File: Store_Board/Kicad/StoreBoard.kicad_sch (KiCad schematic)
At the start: 42 parts, among them J1 Conn_01x10, J2 Conn_01x10, J3 Conn_01x10, J4 Conn_01x10, U1 HM62256BLP, U2 74HCT574, U3 74HCT574, U4 74HCT04, U417 74LS00, U418 74LS00, U419 74LS08, U420 74HC04, U421 74LS112, U422 SN74LS74, U423 74LS10, U424 74LS32

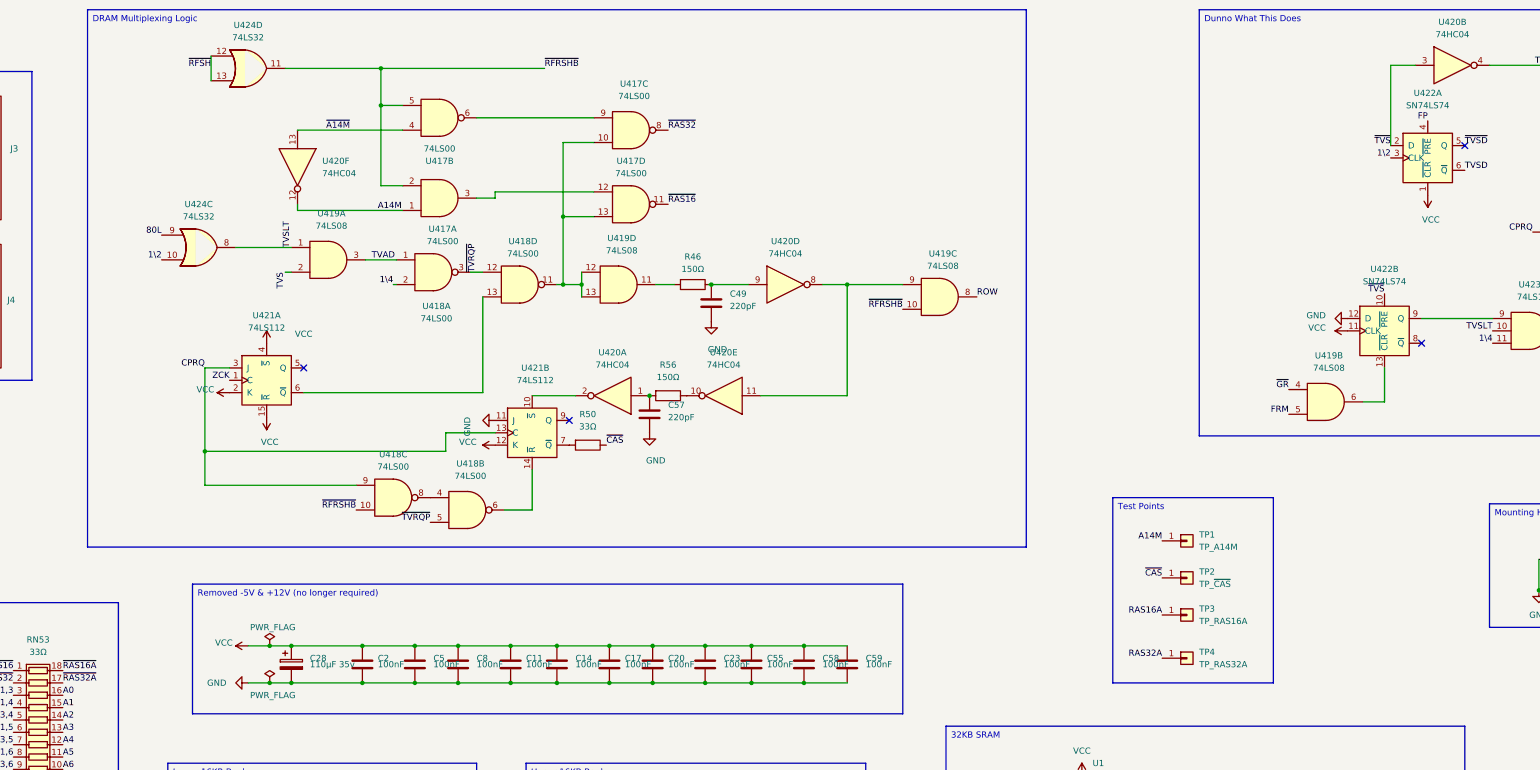
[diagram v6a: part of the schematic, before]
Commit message: Added testpoints
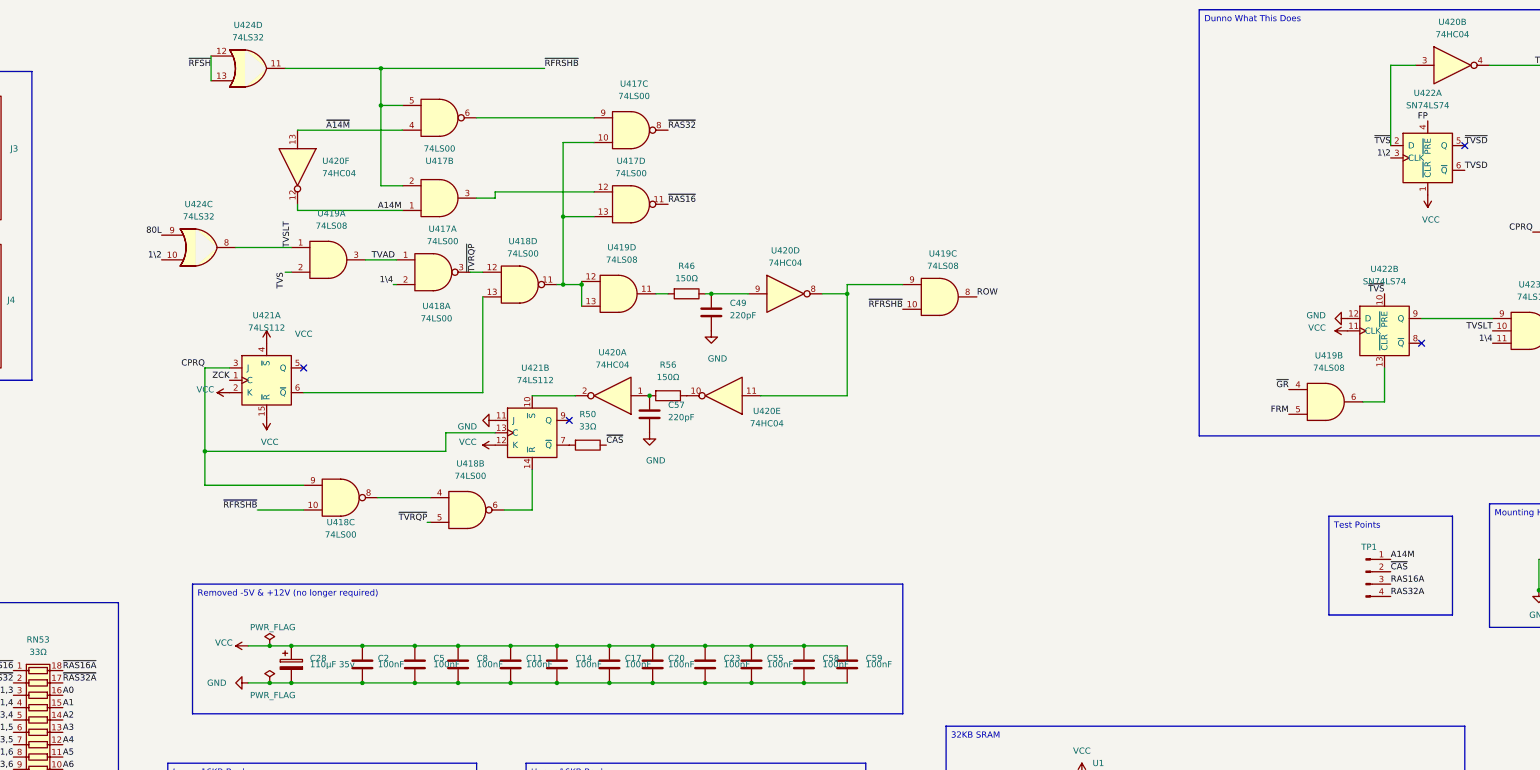
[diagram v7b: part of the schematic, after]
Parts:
- removed TP1: TP_A14M, TestPoint:TestPoint_THTPad_D2.0mm_Drill1.0mm, symbol Connector_Generic:Conn_01x01
- removed TP2: TP_~{CAS}, TestPoint:TestPoint_THTPad_D2.0mm_Drill1.0mm, symbol Connector_Generic:Conn_01x01
- removed TP3: TP_RAS16A, TestPoint:TestPoint_THTPad_D2.0mm_Drill1.0mm, symbol Connector_Generic:Conn_01x01
- removed TP4: TP_RAS32A, TestPoint:TestPoint_THTPad_D2.0mm_Drill1.0mm, symbol Connector_Generic:Conn_01x01
- added TP1: Conn_01x04_Pin, Connector_PinHeader_2.54mm:PinHeader_1x04_P2.54mm_Vertical, symbol Connector:Conn_01x04_Pin
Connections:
- net A14M: now also TP1.1 (Pin_1)
- net RAS16A: now also TP1.3 (Pin_3)
- net RAS32A: now also TP1.4 (Pin_4)
- net ~{CAS}: now also TP1.2 (Pin_2)
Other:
- moved on the sheet: C49, R46, U418C, U419D, U420D

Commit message: Further refinements
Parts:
- removed R50: 33Ω, Resistor_THT:R_Axial_DIN0204_L3.6mm_D1.6mm_P5.08mm_Horizontal, symbol Device:R
- removed RN52: 33Ω, Package_DIP:DIP-16_W7.62mm, symbol Device:R_Pack08
- removed RN53: 33Ω, Package_DIP:DIP-18_W7.62mm, symbol Device:R_Pack09
- removed TP1: Conn_01x04_Pin, Connector_PinHeader_2.54mm:PinHeader_1x04_P2.54mm_Vertical, symbol Connector:Conn_01x04_Pin
- removed U3: 74HCT574, Package_DIP:DIP-20_W7.62mm, symbol 74xx:74HCT574
- removed unit 2 of U4
- added TP1: Conn_02x05_Odd_Even, Connector_PinHeader_2.54mm:PinHeader_2x05_P2.54mm_Vertical, symbol Connector_Generic:Conn_02x05_Odd_Even
- added U3: 74LS32, Package_DIP:DIP-14_W7.62mm, symbol 74xx:74LS32
- C28: value 110µF 35v -> 10µF 35v
- U2: value 74HCT574 -> 74LS574
- U4: value 74HCT04 -> 74LS04
- U420: value 74HC04 -> 74LS04
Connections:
- net RAS_A14 is gone; now on net A14M: U1.1 (A14)
- net ~{RAS16A} is gone; now on net ~{RAS16}: U4.1
- net A14M: now also TP1.1 (Pin_1)
- net GND: now also TP1.10 (Pin_10), TP1.2 (Pin_2), TP1.4 (Pin_4), TP1.6 (Pin_6), TP1.8 (Pin_8), U3.10, U3.12, U3.13, U3.4, U3.5, U3.7 (GND), U3.9; no longer U4.5
- net M1,1: now also RN54.5 (R4), U1.15 (Q3)
- net M2,10: now also RN54.7 (R6), U1.17 (Q5)
- net M4,10: now also RN54.6 (R5), U1.16 (Q4)
- net M4,3: now also RN54.9 (R8), U1.19 (Q7)
- net M4,6: now also RN54.2 (R1), U1.11 (Q0)
- net M4,7: now also RN54.3 (R2), U1.12 (Q1)
- net M4,8: now also RN54.4 (R3), U1.13 (Q2)
- net M4,9: now also RN54.8 (R7), U1.18 (Q6)
- net VCC: now also U3.14 (VCC); no longer RN54.1 (common)
- net ~{CAS}: now also U421.7 (~{Q}), TP1.3 (Pin_3)
- net ~{RAS32}: now also U4.5
- net RAS32: now reaches U4.6
- net RAS32: now also TP1.9 (Pin_9), U3.2
- removed net D0: RN54.9 (R8), U1.11 (Q0)
- removed net D1: RN54.8 (R7), U1.12 (Q1)
- removed net D2: RN54.7 (R6), U1.13 (Q2)
- removed net D3: RN54.6 (R5), U1.15 (Q3)
- removed net D4: RN54.5 (R4), U1.16 (Q4)
- removed net D5: RN54.4 (R3), U1.17 (Q5)
- removed net D6: RN54.3 (R2), U1.18 (Q6)
- removed net D7: RN54.2 (R1), U1.19 (Q7)
- net RAS16A renamed RAS
- net RAS: now also TP1.5 (Pin_5), U3.3; no longer U4.2
- new net RAS16: TP1.7 (Pin_7), U3.1, U4.2
- no-connect marks 10 -> 16
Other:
- note removed: "Or should we use ~{A14M} signal here?"
- note removed: "Use RAS32 to address upper 16KB bank a la A14"
- moved on the sheet: C57, HOLE1, HOLE2, R56, RN54, U1, U2, U420A, U420E, U421B, U423B, U424A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
